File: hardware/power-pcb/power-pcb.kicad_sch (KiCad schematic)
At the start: 40 parts, among them J1 XT60-M-AS, J2 XT30, J3 MicroFit2x12_Odd_Even, J4 MicroFit2x12_CouterClockwise, J5 XT30, J6 XT30, J7 XT30-M-AS, J8 JST_XH_5, Q1 SQJ138EP-T1_GE3, Q2 SQJ138EP-T1_GE3, U1 BTS50010-1TAD, U2 LTC4365TS8, U3 R-78E3.3-1.0

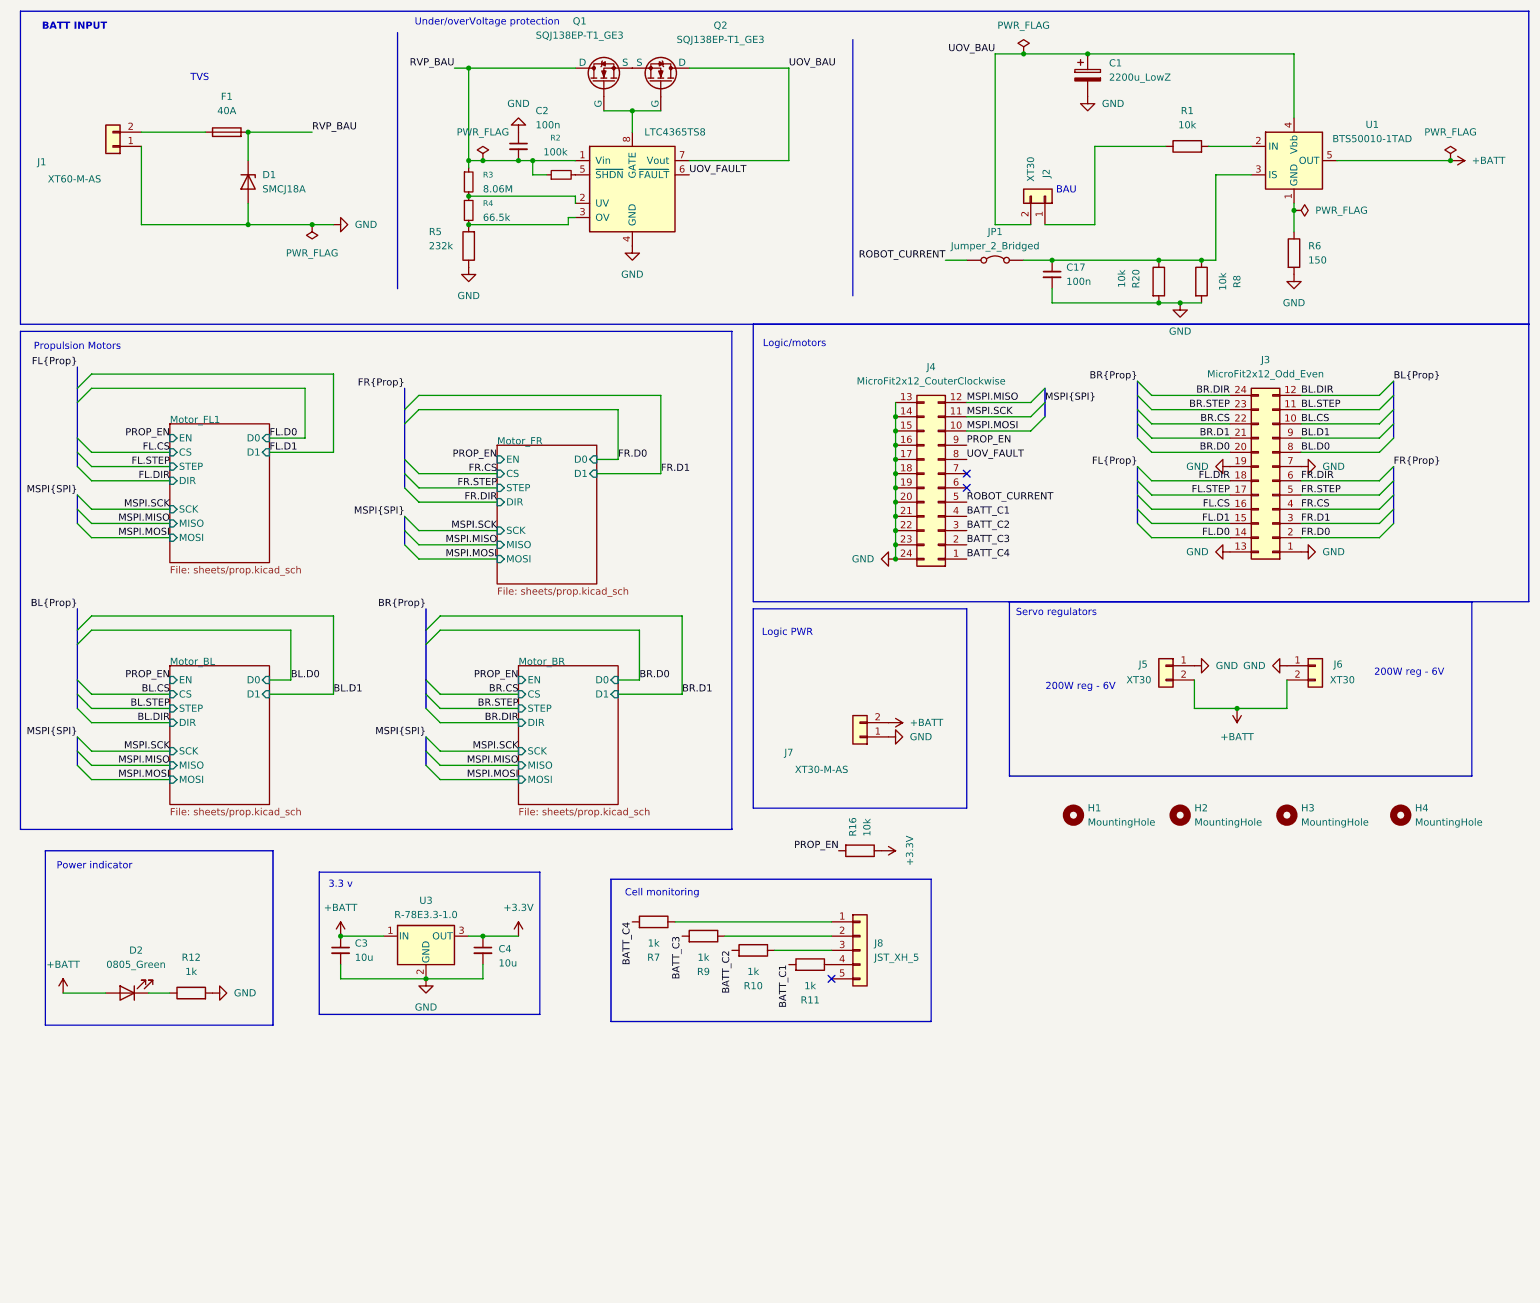
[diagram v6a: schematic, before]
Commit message: Adapt Power PCB to logic requirements
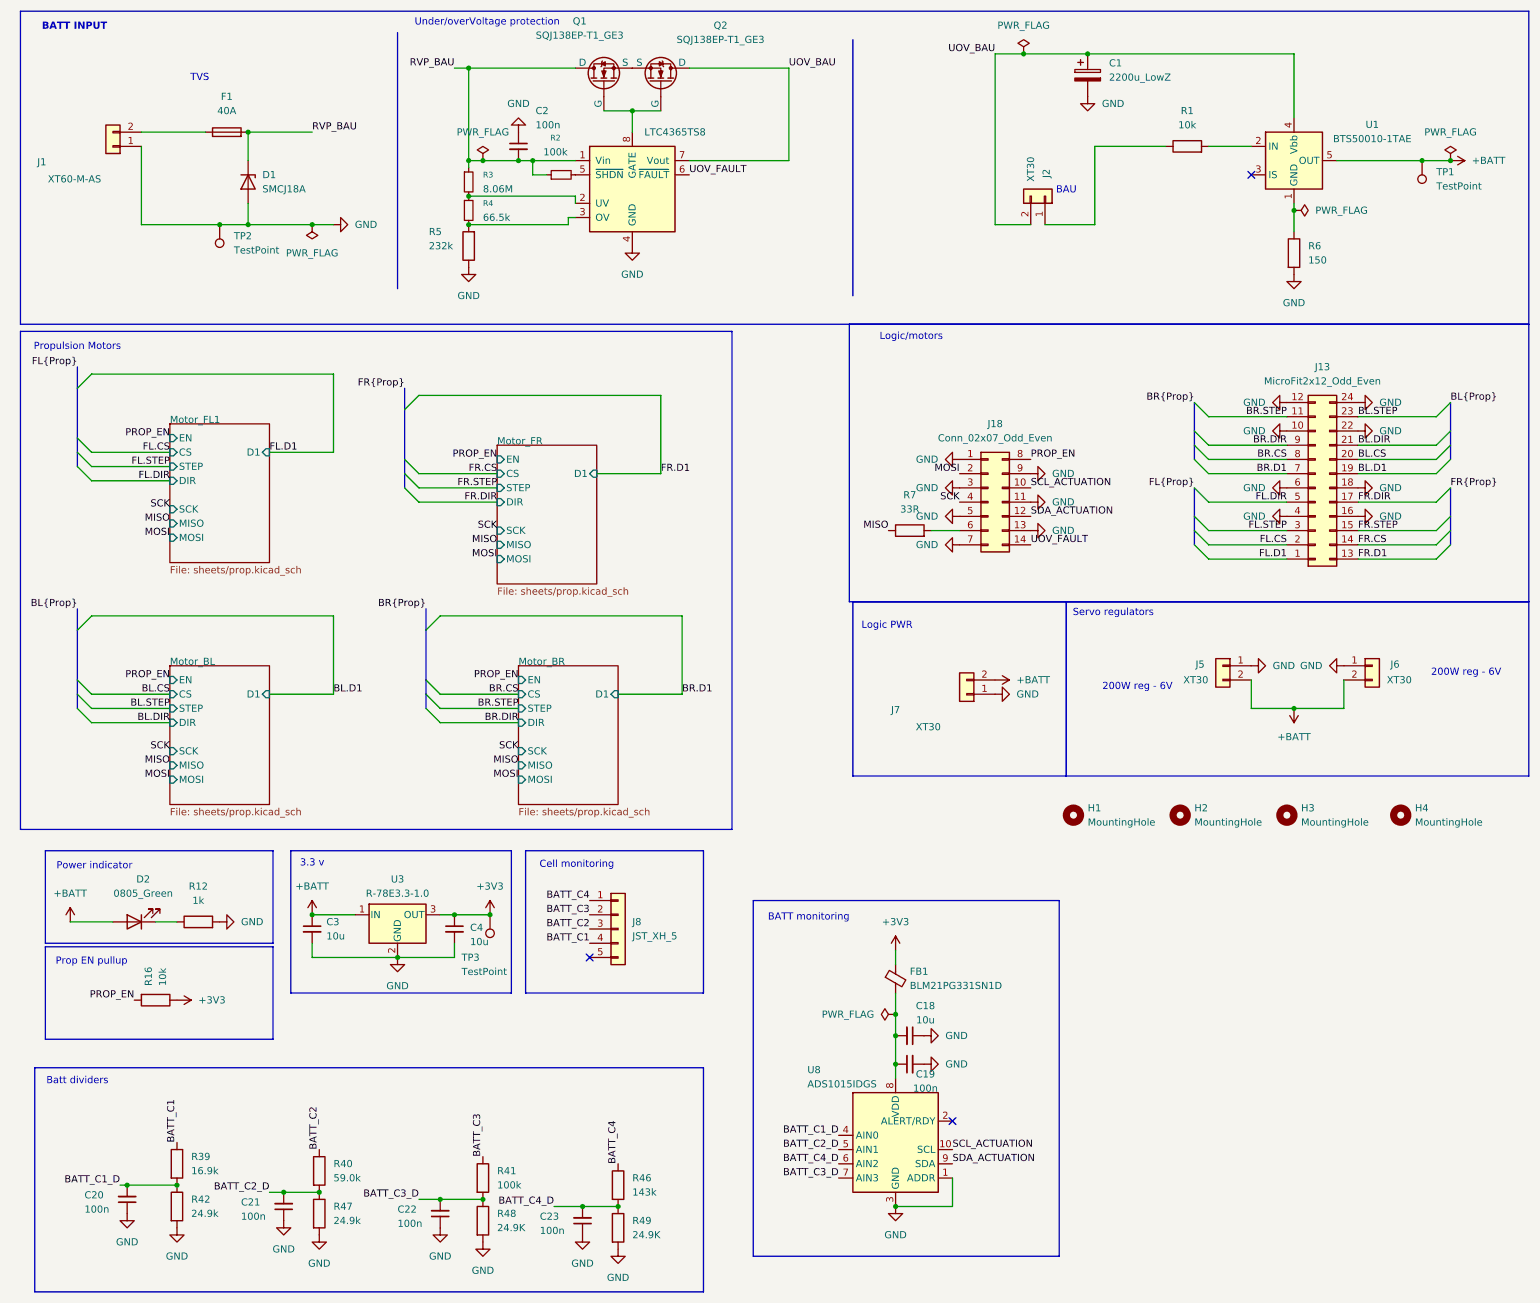
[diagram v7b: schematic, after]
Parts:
- removed C17: 100n, Capacitor_SMD:C_0805_2012Metric_Pad1.18x1.45mm_HandSolder, symbol Device:C_Small
- removed J3: MicroFit2x12_Odd_Even, Project:Molex_Micro-Fit_3.0_43045-2412_2x12_P3.00mm_Vertical, symbol Connector_Generic:Conn_02x12_Top_Bottom
- removed J4: MicroFit2x12_CouterClockwise, Project:Molex_Micro-Fit_3.0_43045-2412_2x12_P3.00mm_Vertical, symbol Connector_Generic:Conn_02x12_Counter_Clockwise
- removed JP1: Jumper_2_Bridged, Project:TestPoint_2Pads_Pitch2.54mm_Drill0.8mm, symbol Jumper:Jumper_2_Bridged
- removed R10, R11, R9: 1k, Resistor_SMD:R_0805_2012Metric_Pad1.20x1.40mm_HandSolder, symbol Device:R
- removed R20, R8: 10k, Resistor_SMD:R_0805_2012Metric_Pad1.20x1.40mm_HandSolder, symbol Device:R
- added C18: 10u, Capacitor_SMD:C_0805_2012Metric_Pad1.18x1.45mm_HandSolder, symbol Device:C_Small
- added C19, C20, C21, C22, C23: 100n, Capacitor_SMD:C_0805_2012Metric_Pad1.18x1.45mm_HandSolder, symbol Device:C_Small
- added FB1: BLM21PG331SN1D, Inductor_SMD:L_0805_2012Metric_Pad1.05x1.20mm_HandSolder, symbol Device:FerriteBead_Small
- added J13: MicroFit2x12_Odd_Even, Project:J_Wurth_WR-MPC3_66202421122, symbol Connector_Generic:Conn_02x12_Top_Bottom
- added J18: Conn_02x07_Odd_Even, Project:J_Wurth_WR-MPC3_66201421122, symbol Connector_Generic:Conn_02x07_Top_Bottom
- added R39: 16.9k, Resistor_SMD:R_0805_2012Metric_Pad1.20x1.40mm_HandSolder, symbol Device:R
- added R40: 59.0k, Resistor_SMD:R_0805_2012Metric_Pad1.20x1.40mm_HandSolder, symbol Device:R
- added R41: 100k, Resistor_SMD:R_0805_2012Metric_Pad1.20x1.40mm_HandSolder, symbol Device:R
- added R42, R47: 24.9k, Resistor_SMD:R_0805_2012Metric_Pad1.20x1.40mm_HandSolder, symbol Device:R
- added R46: 143k, Resistor_SMD:R_0805_2012Metric_Pad1.20x1.40mm_HandSolder, symbol Device:R
- added R48, R49: 24.9K, Resistor_SMD:R_0805_2012Metric_Pad1.20x1.40mm_HandSolder, symbol Device:R
- added TP1, TP2, TP3: TestPoint, TestPoint:TestPoint_THTPad_D1.0mm_Drill0.5mm, symbol Connector:TestPoint
- added U8: ADS1015IDGS, Package_SO:TSSOP-10_3x3mm_P0.5mm, symbol Analog_ADC:ADS1015IDGS
- J7: value XT30-M-AS -> XT30
- R2: MPN CRCW0805100KFKEA -> CRCW0805100K0FKEA
- R7: value 1k -> 33R; MPN CRCW08051K00FKEA -> CRCW080533RFKEA
- U1: value BTS50010-1TAD -> BTS50010-1TAE; MPN BTS500101TADATMA2 -> BTS500101TAEATMA1
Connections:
- net +BATT: now also TP1.1
- net BATT_C1: now also J8.4 (Pin_4), R39.1
- net BATT_C2: now also J8.3 (Pin_3), R40.1
- net BATT_C3: now also J8.2 (Pin_2), R41.1
- net BATT_C4: now also J8.1 (Pin_1), R46.1; no longer R7.2
- net BL.CS: now also J13.20 (Pin_20)
- net BL.D1: now also J13.19 (Pin_19)
- net BL.DIR: now also J13.21 (Pin_21)
- net BL.STEP: now also J13.23 (Pin_23)
- net BR.CS: now also J13.8 (Pin_8)
- net BR.D1: now also J13.7 (Pin_7)
- net BR.DIR: now also J13.9 (Pin_9)
- net BR.STEP: now also J13.11 (Pin_11)
- net FL.CS: now also J13.2 (Pin_2)
- net FL.D1: now also J13.1 (Pin_1)
- net FL.DIR: now also J13.5 (Pin_5)
- net FL.STEP: now also J13.3 (Pin_3)
- net FR.CS: now also J13.14 (Pin_14)
- net FR.D1: now also J13.13 (Pin_13)
- net FR.DIR: now also J13.17 (Pin_17)
- net FR.STEP: now also J13.15 (Pin_15)
- net GND: now also C18.1, C19.2, C20.1, C21.1, C22.1, C23.1, J13.10 (Pin_10), J13.12 (Pin_12), J13.16 (Pin_16), J13.18 (Pin_18), J13.22 (Pin_22), J13.24 (Pin_24), J13.4 (Pin_4), J13.6 (Pin_6), J18.1 (Pin_1), J18.11 (Pin_11), J18.13 (Pin_13), J18.3 (Pin_3), J18.5 (Pin_5), J18.7 (Pin_7), J18.9 (Pin_9), R42.2, R47.2, R48.2, R49.2, TP2.1, U8.1 (ADDR), U8.3 (GND)
- net PROP_EN: now also J18.8 (Pin_8)
- net UOV_FAULT: now also J18.14 (Pin_14)
- net MISO: now reaches R7.1
- net MISO: no longer J8.1 (Pin_1)
- net +3.3V renamed +3V3
- net +3V3: now also FB1.1, TP3.1
- new net: C18.2, C19.1, FB1.2, U8.8 (VDD)
- new net: J18.6 (Pin_6), R7.2
- new net BATT_C1_D: C20.2, R39.2, R42.1, U8.4 (AIN0)
- new net BATT_C2_D: C21.2, R40.2, R47.1, U8.5 (AIN1)
- new net BATT_C3_D: C22.2, R41.2, R48.1, U8.7 (AIN3)
- new net BATT_C4_D: C23.2, R46.2, R49.1, U8.6 (AIN2)
- new net MOSI: J18.2 (Pin_2)
- new net SCK: J18.4 (Pin_4)
- new net SCL_ACTUATION: J18.10 (Pin_10), U8.10 (SCL)
- new net SDA_ACTUATION: J18.12 (Pin_12), U8.9 (SDA)
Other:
- sheet Motor_BL ports: added none; removed D0
- sheet Motor_BR ports: added none; removed D0
- sheet Motor_FL1 ports: added none; removed D0
- sheet Motor_FR ports: added none; removed D0
- note added: "BATT monitoring"
- note added: "Batt dividers"
- note added: "Prop EN pullup"
- moved on the sheet: C3, C4, D2, J5, J6, J7, J8, R12, R16, U3

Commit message: fixes pre-prod
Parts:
- J13: MPN 66202421122 -> 43045-2412; Manufacturer Wurth -> Molex
- J18: MPN 66201421122 -> 43045-1412; Manufacturer Wurth -> Molex
- J2, J5, J6, J7: footprint Project:AMASS_XT30UPB-M_1x02_P5.0mm_Vertical -> Project:AMASS_XT30U-M_1x02_P5.0mm_Vertical
- R2, R41: MPN CRCW0805100K0FKEA -> CRCW0805100KFKEA
- R46: MPN CRCW0805143K0FKEA -> CRCW0805143KFKEA
- R7: MPN CRCW080533RFKEA -> CRCW080533R0FKEA
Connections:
- net MOSI: now also J18.6 (Pin_6); no longer J18.2 (Pin_2)
- net PROP_EN: now also J18.14 (Pin_14); no longer J18.8 (Pin_8)
- net SCL_ACTUATION: now also J18.12 (Pin_12); no longer J18.10 (Pin_10)
- net SDA_ACTUATION: now also J18.10 (Pin_10); no longer J18.12 (Pin_12)
- net UOV_FAULT: now also J18.8 (Pin_8); no longer J18.14 (Pin_14)
- net at R7.2: now also J18.2 (Pin_2); no longer J18.6 (Pin_6)
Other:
- moved on the sheet: R7
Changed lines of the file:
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@@
 	(wire
 		(pts
-			(xy 176.53 106.68) (xy 181.61 106.68)
+			(xy 175.26 106.68) (xy 181.61 106.68)
 		)
 		(stroke
@@
 	)
 	(label "MISO"
-		(at 168.91 106.68 180)
+		(at 167.64 106.68 180)
 		(effects
 			(font
@@
 			)
 		)
-		(property "MPN" "CRCW0805143K0FKEA"
+		(property "MPN" "CRCW0805143KFKEA"
 			(at 120.65 223.52 0)
 			(effects
@@
 			)
 		)
-		(property "MPN" "66202421122"
+		(property "MPN" "43045-2412"
 			(at 245.11 99.06 0)
 			(effects
@@
 			)
 		)
-		(property "Manufacturer" "Wurth"
+		(property "Manufacturer" "Molex"
 			(at 245.11 99.06 0)
 			(effects
@@
 			)
 		)
-		(property "Footprint" "Project:AMASS_XT30UPB-M_1x02_P5.0mm_Vertical"
+		(property "Footprint" "Project:AMASS_XT30U-M_1x02_P5.0mm_Vertical"
 			(at 228.6 130.81 0)
 			(effects
@@
 			)
 		)
-		(property "Footprint" "Project:AMASS_XT30UPB-M_1x02_P5.0mm_Vertical"
+		(property "Footprint" "Project:AMASS_XT30U-M_1x02_P5.0mm_Vertical"
 			(at 182.88 135.89 0)
 			(effects
@@
 			)
 		)
-		(property "MPN" "CRCW0805100K0FKEA"
+		(property "MPN" "CRCW0805100KFKEA"
 			(at 96.52 222.25 0)
 			(effects
@@
 	(symbol
 		(lib_id "Device:R")
-		(at 172.72 106.68 90)
+		(at 171.45 106.68 90)
 		(unit 1)
 		(exclude_from_sim no)
@@
 		(fields_autoplaced yes)
 		(property "Reference" "R7"
-			(at 172.72 100.33 90)
+			(at 171.45 100.33 90)
 			(effects
 				(font
@@
 		)
 		(property "Value" "33R"
-			(at 172.72 102.87 90)
+			(at 171.45 102.87 90)
 			(effects
 				(font
@@
 		)
 		(property "Footprint" "Resistor_SMD:R_0805_2012Metric_Pad1.20x1.40mm_HandSolder"
-			(at 172.72 108.458 90)
+			(at 171.45 108.458 90)
 			(effects
 				(font
@@
 		)
 		(property "Datasheet" "~"
-			(at 172.72 106.68 0)
+			(at 171.45 106.68 0)
 			(effects
 				(font
@@
 		)
 		(property "Description" "Resistor"
-			(at 172.72 106.68 0)
+			(at 171.45 106.68 0)
 			(effects
 				(font
@@
 			)
 		)
-		(property "MPN" "CRCW080533RFKEA"
-			(at 172.72 106.68 90)
+		(property "MPN" "CRCW080533R0FKEA"
+			(at 171.45 106.68 90)
 			(effects
 				(font
@@
 		)
 		(property "Manufacturer" "Vishay"
-			(at 172.72 106.68 90)
+			(at 171.45 106.68 90)
 			(effects
 				(font
@@
 			)
 		)
-		(property "Footprint" "Project:AMASS_XT30UPB-M_1x02_P5.0mm_Vertical"
+		(property "Footprint" "Project:AMASS_XT30U-M_1x02_P5.0mm_Vertical"
 			(at 255.27 130.81 0)
 			(effects
@@
 		(lib_id "Connector_Generic:Conn_02x07_Top_Bottom")
 		(at 186.69 101.6 0)
+		(mirror x)
 		(unit 1)
 		(exclude_from_sim no)
@@
 		(on_board yes)
 		(dnp no)
-		(fields_autoplaced yes)
 		(property "Reference" "J18"
-			(at 187.96 87.63 0)
+			(at 187.96 115.57 0)
 			(effects
 				(font
@@
 		)
 		(property "Value" "Conn_02x07_Odd_Even"
-			(at 187.96 90.17 0)
+			(at 187.96 113.03 0)
 			(effects
 				(font
@@
 			)
 		)
-		(property "MPN" "66201421122"
+		(property "MPN" "43045-1412"
 			(at 186.69 101.6 0)
 			(effects
@@
 			)
 		)
-		(property "Manufacturer" "Wurth"
+		(property "Manufacturer" "Molex"
 			(at 186.69 101.6 0)
 			(effects
@@
 			)
 		)
-		(property "Footprint" "Project:AMASS_XT30UPB-M_1x02_P5.0mm_Vertical"
+		(property "Footprint" "Project:AMASS_XT30U-M_1x02_P5.0mm_Vertical"
 			(at 196.85 46.99 0)
 			(effects
@@
 			)
 		)
-		(property "MPN" "CRCW0805100K0FKEA"
+		(property "MPN" "CRCW0805100KFKEA"
 			(at 110.49 43.18 90)
 			(effects
